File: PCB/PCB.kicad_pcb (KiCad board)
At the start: 2 copper layers, 43.2 x 71.1 mm, 20 parts, among them J1 Conn_01x04_Female, J2 Conn_01x05_Female, J3 Screw_Terminal_01x02, J4 Conn_01x03_Female, J5 Conn_01x03_Female, J6 Conn_01x03_Female, J7 Conn_01x03_Female, U1 R-785.0-1.0

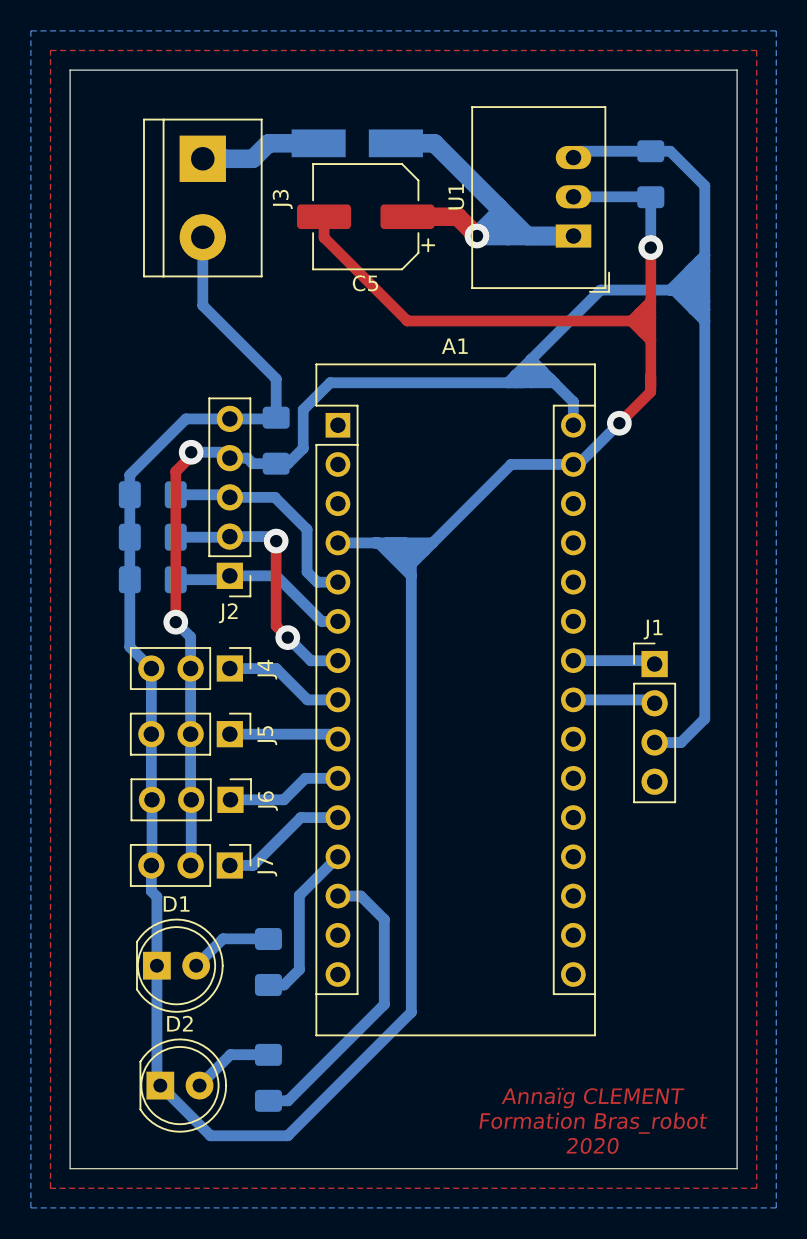
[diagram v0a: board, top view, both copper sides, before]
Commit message: MAJ : Mounting holes
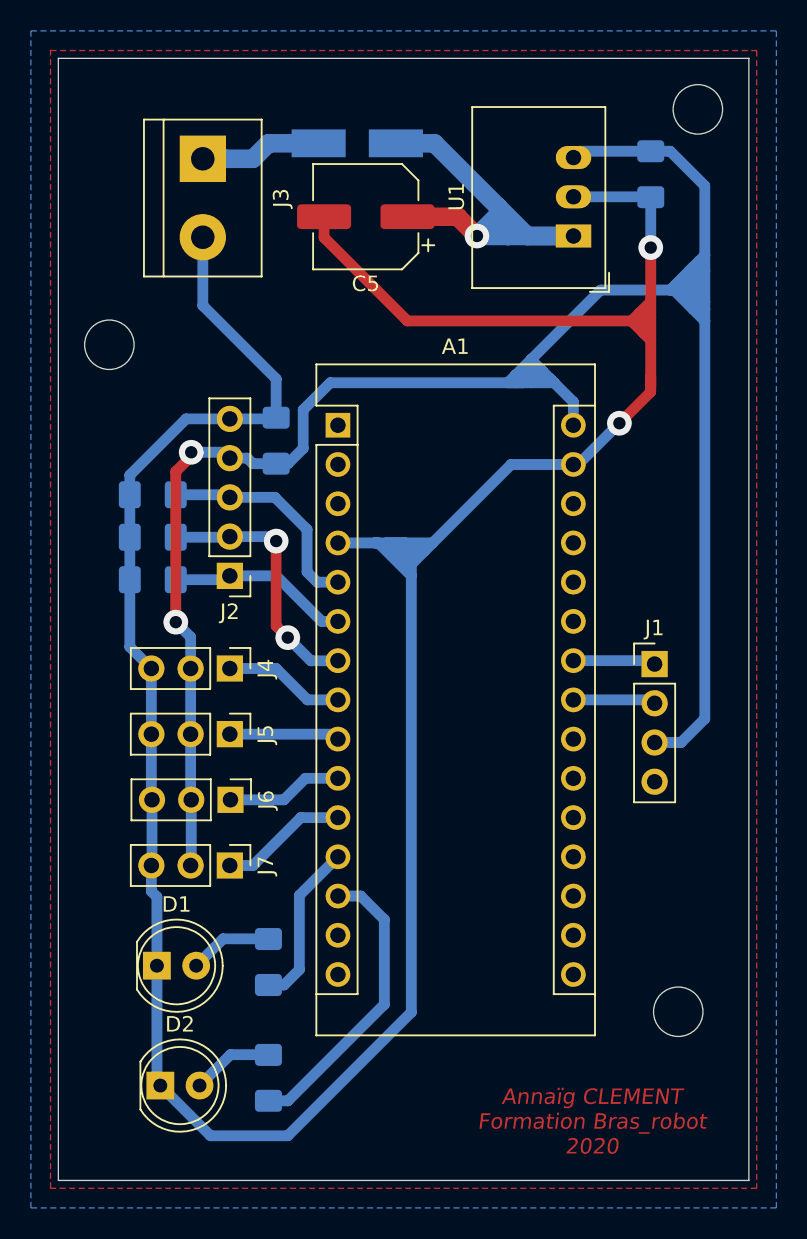
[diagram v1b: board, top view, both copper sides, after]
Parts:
- added ?: MountingHole_3.2mm_M3, MountingHole:MountingHole_3.2mm_M3, F.Cu at (146.1, 50.8)
- added ?: MountingHole_3.2mm_M3, MountingHole:MountingHole_3.2mm_M3, F.Cu at (144.8, 109.2)
- added ?: MountingHole_3.2mm_M3, MountingHole:MountingHole_3.2mm_M3, F.Cu at (108.0, 66.0)
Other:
- board size 43.2 x 71.1 mm -> 44.7 x 72.6 mm

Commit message: Add files via upload
MàJ
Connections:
- A1 pad 27: Net-(A1-Pad27) -> +5V
- A1 pad 30: +5V -> Net-(A1-Pad30)
